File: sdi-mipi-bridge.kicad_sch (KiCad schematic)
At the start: 203 parts, among them J1 112740-13, J2 112740-13, J3 WE_68715014522_ONE-SIDE, J4 GRPB052VWVN-RC, J5 GRPB041VWVN-RC, J6 GRPB052VWVN-RC, SW1 SW_DIP_x06, SW2 SW_DIP_x06, U1 MAX8902B, U2 GS2971A, U3 GS2988, U4 CrossLink_LIF-MD6000-6JMG80I, U5 SC18IS602BIPW, Y1 ABM7_27.000MH_D2Y_T

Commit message: Tidy up the schematic
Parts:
- R89: DNP 1 -> DNP
- gave numbers to parts that had none: 12
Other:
- note removed: "DNP"
- moved on the sheet: J6, N1, N2, U2C

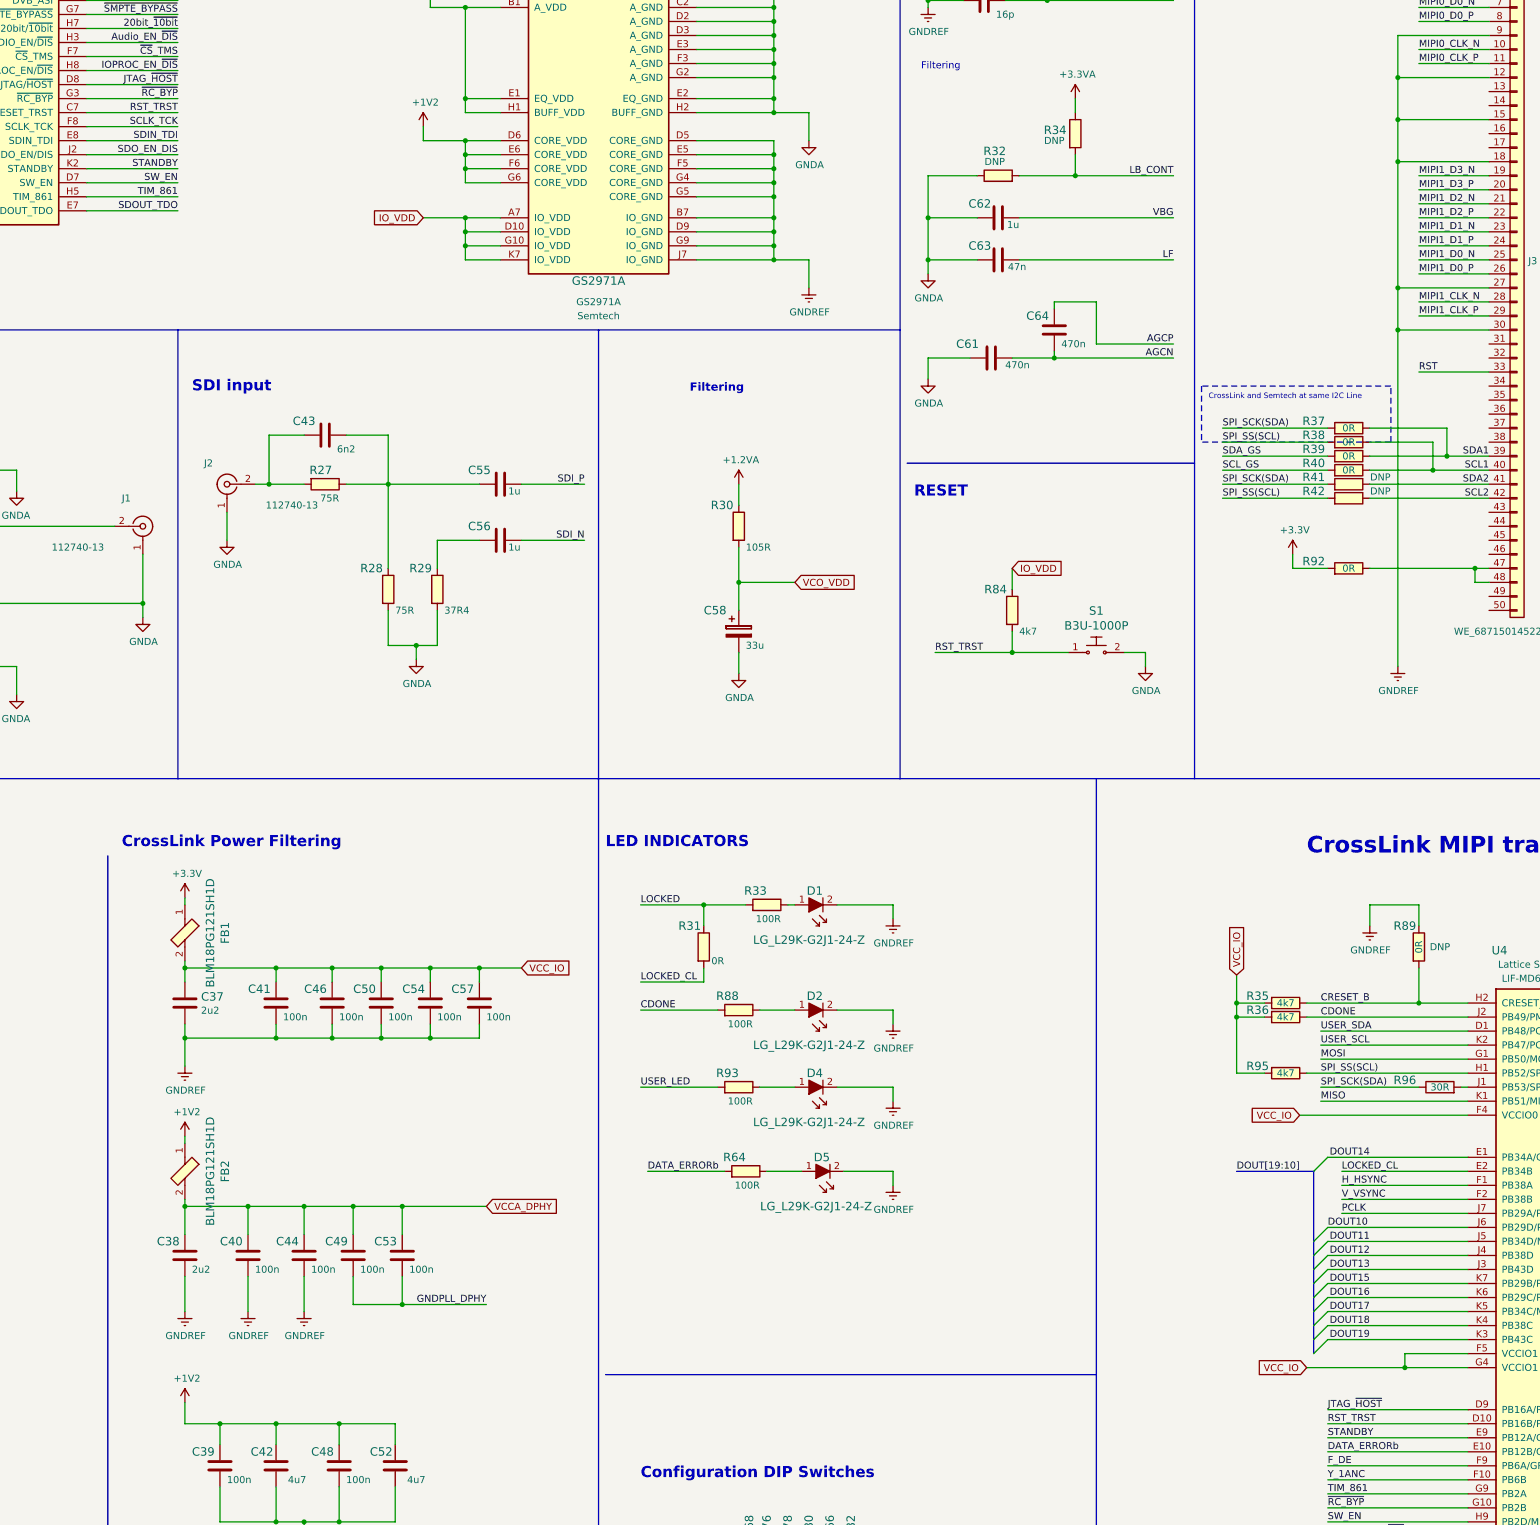
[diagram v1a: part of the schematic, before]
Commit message: Improved RST_TRST circuit
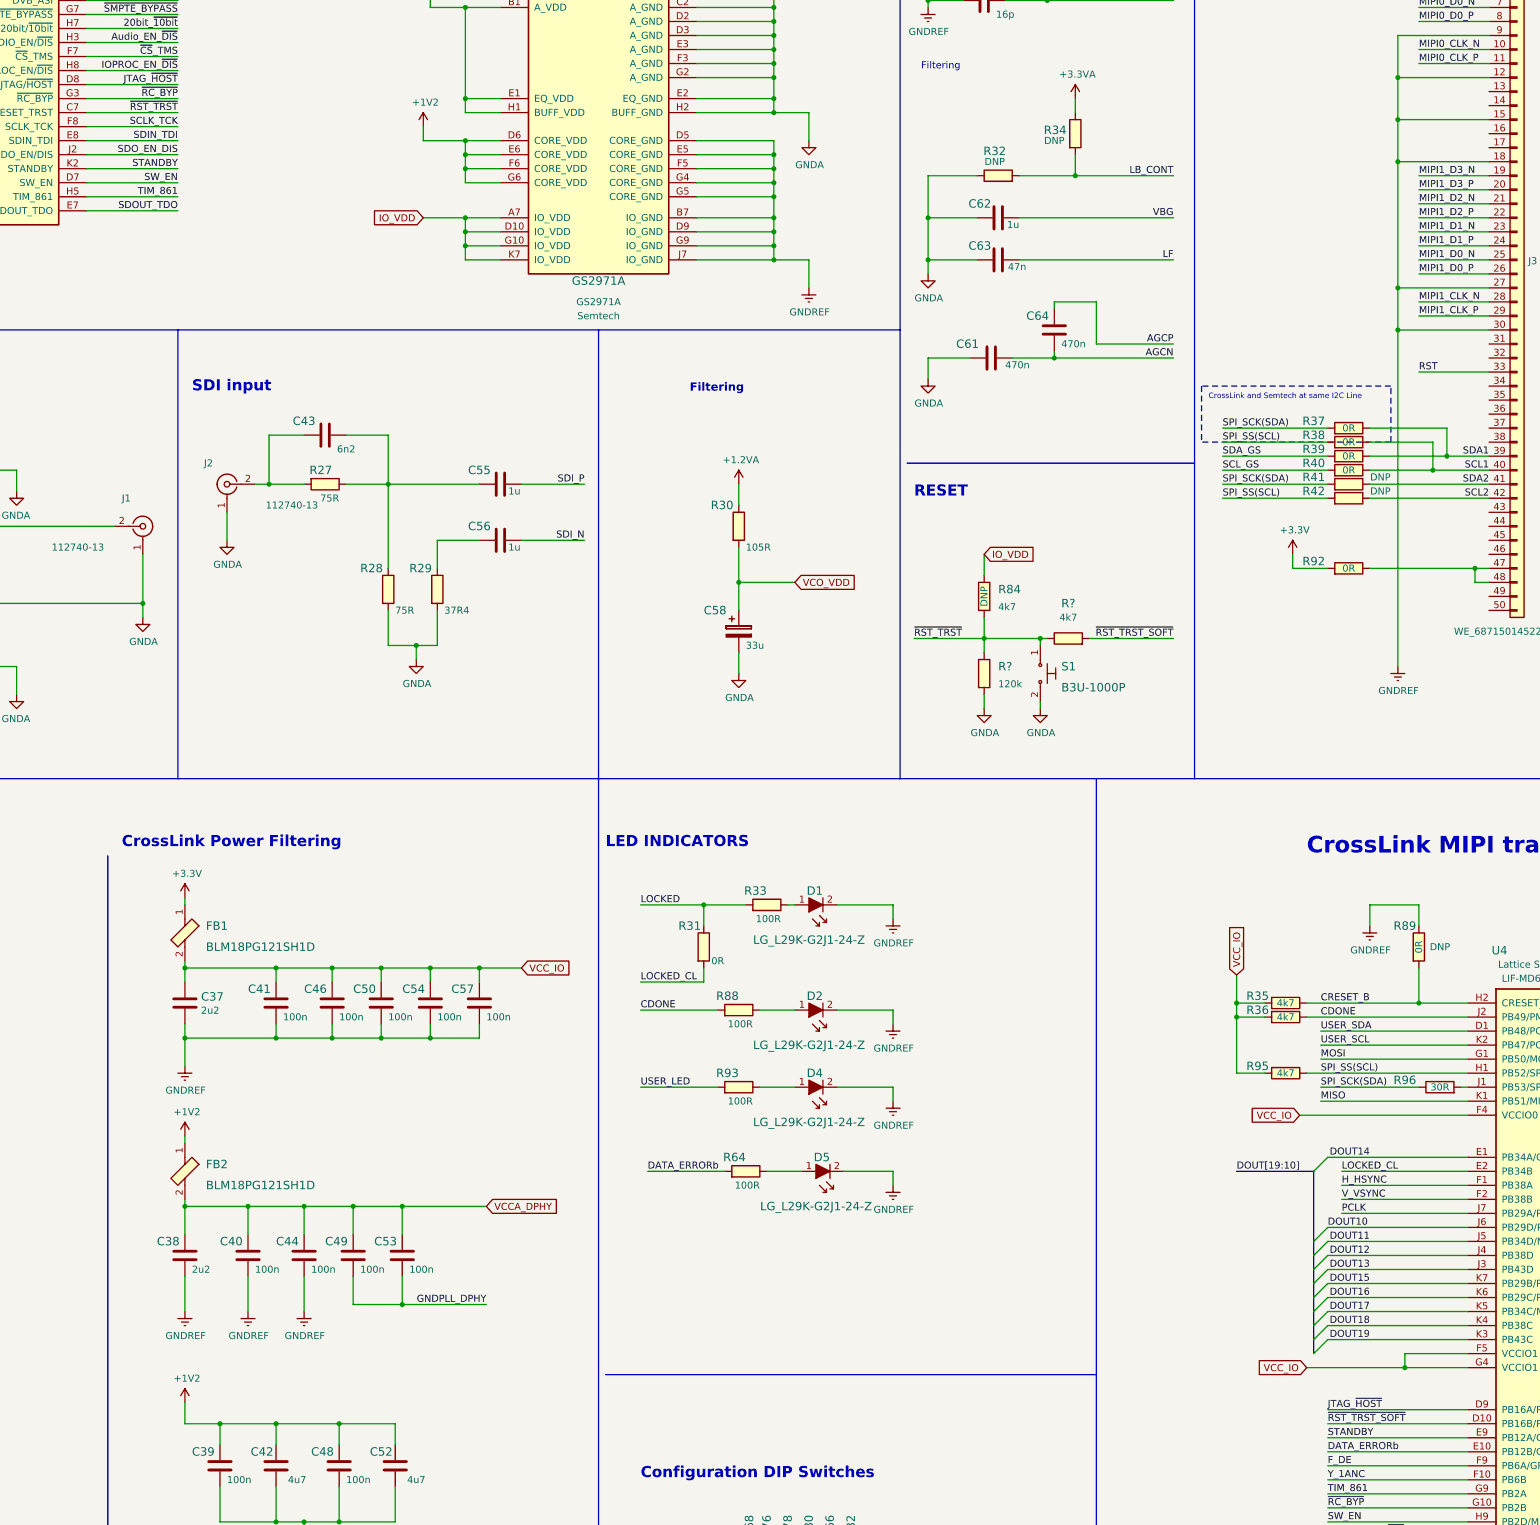
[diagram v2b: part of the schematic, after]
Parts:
- added R?: R_4k7_0402, sdi-mipi-bridge-footprints:0402-res, symbol sdi-mipi-bridge:R_4k7_0402
- added R?: R_120k_0402, sdi-mipi-bridge-footprints:0402-res, symbol sdi-mipi-bridge:R_120k_0402
- R84: DNP (none) -> DNP
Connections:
- net GNDA: now also R?.2
- net RST_TRST renamed ~{RST_TRST}
- net ~{RST_TRST}: now also R?.1, R?.1; no longer U4.D10 (PB16B/PCLKC2_0)
- new net ~{RST_TRST_SOFT}: R?.2, U4.D10 (PB16B/PCLKC2_0)
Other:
- moved on the sheet: R84, S1

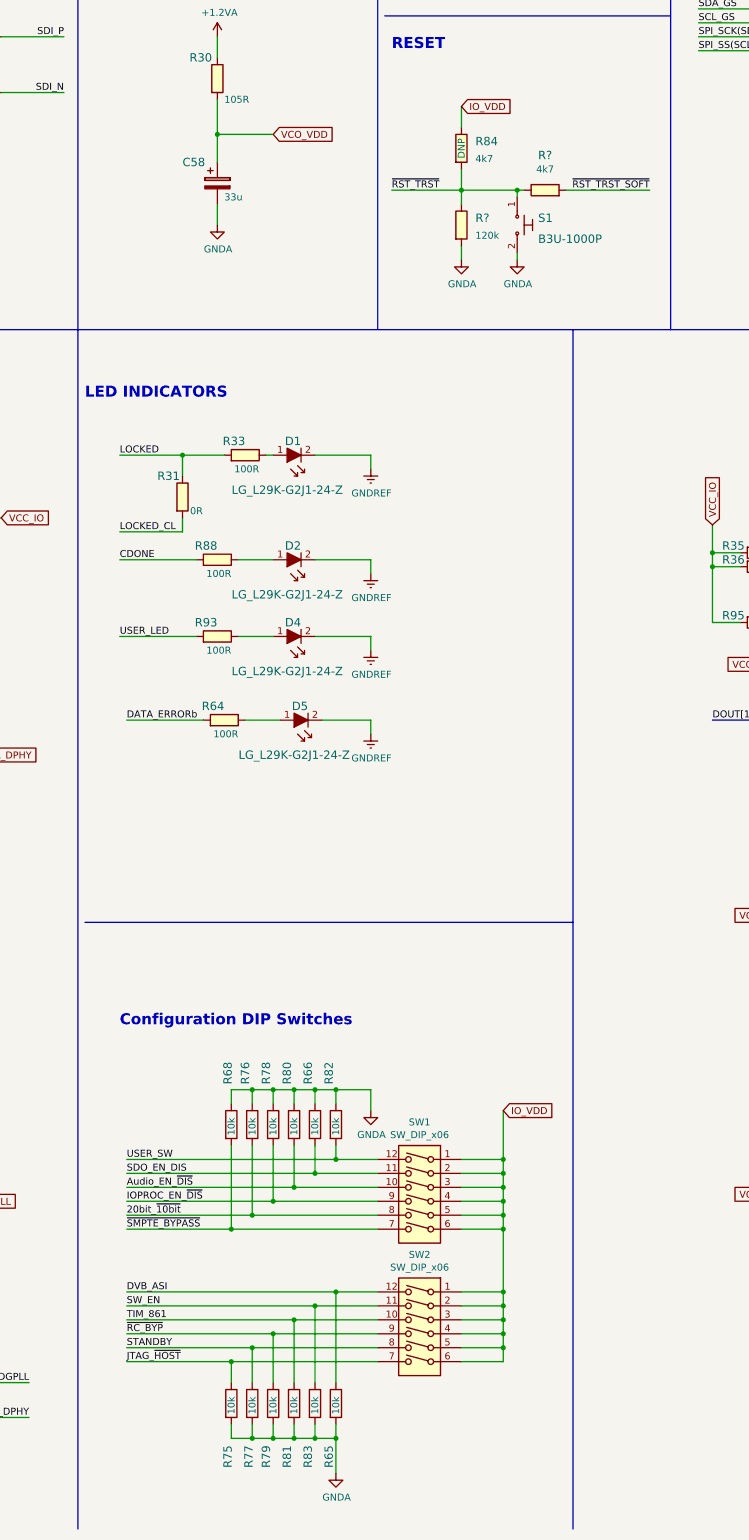
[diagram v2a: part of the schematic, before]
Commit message: Fixed DIP switches shorting FPGA to IO_VDD
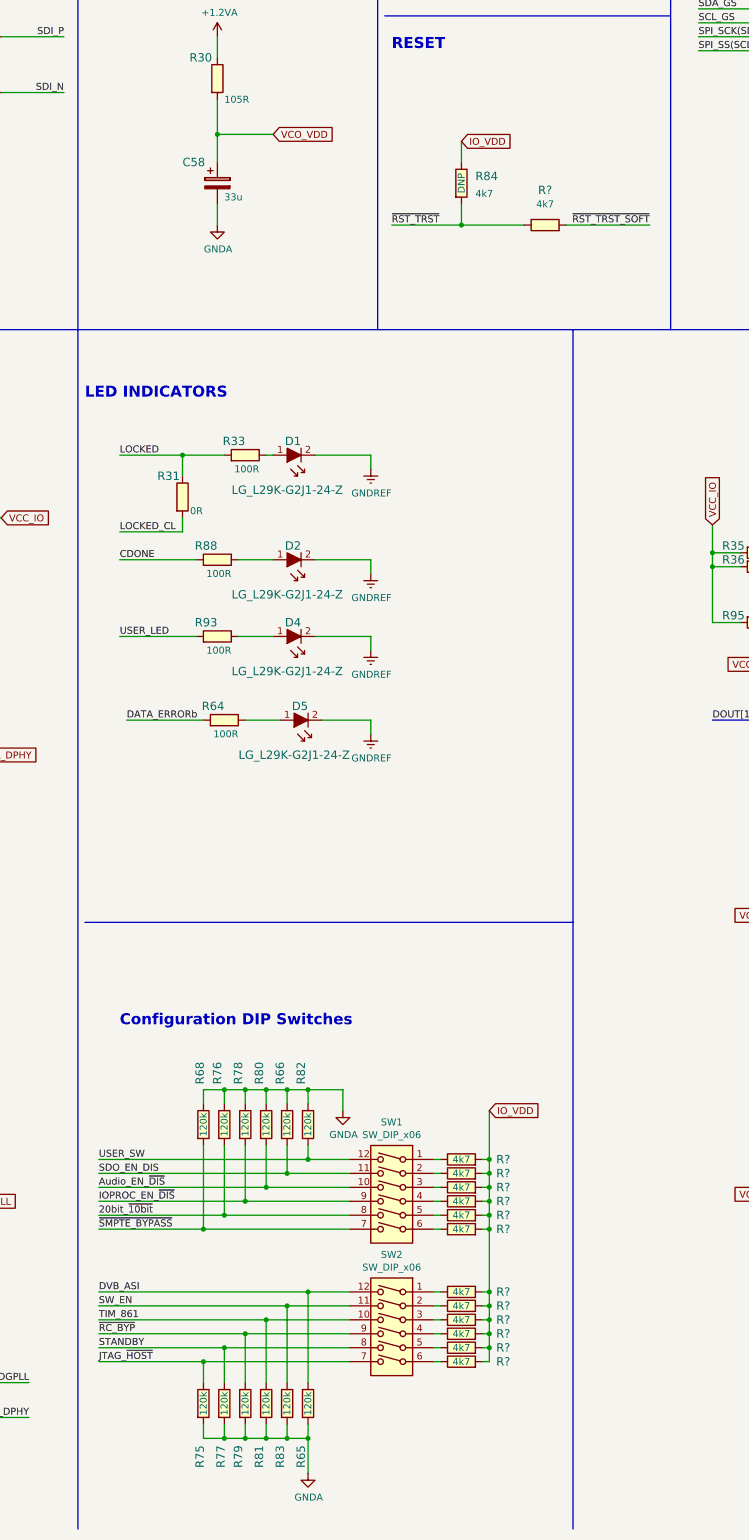
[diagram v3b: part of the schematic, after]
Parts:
- removed R?: R_120k_0402, sdi-mipi-bridge-footprints:0402-res, symbol sdi-mipi-bridge:R_120k_0402
- removed S1: B3U-1000P, sdi-mipi-bridge-footprints:Switch_Tactile_SMD_B3U-1000P, symbol sdi-mipi-bridge:B3U-1000P
- added R? (x12): R_4k7_0402, sdi-mipi-bridge-footprints:0402-res, symbol sdi-mipi-bridge:R_4k7_0402
- R65, R66, R68, R75, R76, R77, R78, R79, R80, R81, R82, R83: value R_10k_0402 -> R_120k_0402; symbol sdi-mipi-bridge:R_10k_0402 -> sdi-mipi-bridge:R_120k_0402; MPN CRCW040210K0FKEDHP -> CRCW0402120KFKED; Val 10k -> 120k
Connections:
- net IO_VDD: now also R?.2, R?.2, R?.2, R?.2, R?.2, R?.2, R?.2, R?.2, R?.2, R?.2, R?.2, R?.2; no longer SW1.1, SW1.2, SW1.3, SW1.4, SW1.5, SW1.6, SW2.1, SW2.2, SW2.3, SW2.4, SW2.5, SW2.6
- new net: R?.1, SW1.1
- new net: R?.1, SW1.2
- new net: R?.1, SW1.3
- new net: R?.1, SW1.4
- new net: R?.1, SW1.5
- new net: R?.1, SW1.6
- new net: R?.1, SW2.1
- new net: R?.1, SW2.2
- new net: R?.1, SW2.3
- new net: R?.1, SW2.4
- new net: R?.1, SW2.5
- new net: R?.1, SW2.6
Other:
- moved on the sheet: R84, R?, SW1, SW2
